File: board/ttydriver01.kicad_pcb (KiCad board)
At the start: 2 copper layers, 119.4 x 74.9 mm, 61 parts, among them J1 PRINTER JACK, J2 KEYBOARD JACK, J3 MOTOR CTL RELAY JACK, P1 CONN_01X02, SW1 Switch_SPDT, SW2 Button_SPDT, T1 Coilcraft-FA2469-AL, U1 NE555, U2 AP2553W6, U3 CP2102-breakout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

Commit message: First try at 2.1 autorouting
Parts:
- removed D12: 4.7V Zener, Diodes_SMD:SOD-123
- removed REF1, REF2, REF3, REF4: MountingHole_2.7mm_M2.5, Mounting_Holes:MountingHole_2.7mm_M2.5
- removed REF5: Fiducial_classic_Small_SilkscreenTop_Type1, Fiducials:Fiducial_classic_Small_SilkscreenTop_Type1
- added R17: 510, Resistors_SMD:R_1206, F.Cu at (145.5, 114.6)
- added R18: 2.2K, Resistors_SMD:R_1206, F.Cu at (159.8, 95.5)
- added W5: TEST_1P, Pin_Headers:Pin_Header_Straight_1x01_Pitch2.54mm, F.Cu at (127.3, 143.8)
- C2: footprint Capacitors_SMD:C_0805 -> Capacitors_ThroughHole:C_Disc_D6.0mm_W4.4mm_P5.00mm
- C8: value 880pf -> 910pf
- R6: value 720 -> 715
- R7: value 7.2K -> 7.15K
- W1, W2, W3, W4: footprint Connect:PINTST -> Pin_Headers:Pin_Header_Straight_1x01_Pitch2.54mm
- moved R16 50.0 mm to (148.3, 95.8), turned to 270 degrees
- moved T1 3.59 mm to (130.0, 123.4)
- moved U9 3.06 mm to (129.3, 136.7)
- moved C4 2.29 mm to (127.5, 131.8)
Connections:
- C1 pad 1: VCC -> Net-(C1-Pad1)
- C9 pad 1: VCC -> Net-(C1-Pad1)
- D13 pad 5: Net-(D12-Pad2) -> GND
- L3 pad 1: VCC -> Net-(C1-Pad1)
- R10 pad 2: Net-(D12-Pad1) -> /TxD
- R12 pad 2: VCC -> Net-(C1-Pad1)
- R5 pad 2: Net-(D12-Pad2) -> Net-(R5-Pad2)
- R6 pad 2: VCC -> Net-(C1-Pad1)
- U1 pad 4: VCC -> Net-(C1-Pad1)
- U1 pad 8: VCC -> Net-(C1-Pad1)
- U2 pad 6: VCC -> Net-(C1-Pad1)
- U3 pad 2-4: VCC -> Net-(C1-Pad1)
- U5 pad 2: VCC -> Net-(C1-Pad1)
- U6 pad 4: /RxD -> Net-(C1-Pad1)
- U6 pad 5: VCC -> /RxD
- U6 pad 6: /RxD -> Net-(C1-Pad1)
- U7 pad 1: Net-(U3-Pad3-5) -> Net-(R17-Pad2)
- U7 pad 2: GND -> Net-(U3-Pad3-5)
- U7 pad 4: VCC -> Net-(C1-Pad1)
- U7 pad 6: VCC -> Net-(C1-Pad1)
- U8 pad 2: VCC -> Net-(C1-Pad1)
- U8 pad 4: Net-(D12-Pad1) -> Net-(R5-Pad2)
- W1 pad 1: VCC -> Net-(C1-Pad1)
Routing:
- net GND: track 333.8 -> 0.00 mm, vias 1 -> 0
- net VCC: track 234.2 -> 0.00 mm, vias 3 -> 0
- net /HVNEG: track 180.0 -> 0.00 mm
- net Net-(J3-PadT): track 115.6 -> 0.00 mm
- net /ENABLE: track 106.9 -> 0.00 mm
- net Net-(J2-PadS): track 92.2 -> 0.00 mm, vias 1 -> 0
- net Net-(C3-Pad1): track 90.9 -> 0.00 mm, vias 2 -> 0
- net Net-(SW1-Pad2): track 72.2 -> 0.00 mm
- net Net-(R18-Pad1): track 70.1 -> 0.00 mm
- net Net-(R16-Pad1): track 62.5 -> 0.00 mm, vias 2 -> 0
- net Net-(D12-Pad2): track 58.3 -> 0.00 mm, vias 1 -> 0
- net /RxD: track 55.7 -> 0.00 mm
- net Net-(R13-Pad2): track 52.3 -> 0.00 mm, vias 2 -> 0
- net Net-(D12-Pad1): track 52.2 -> 0.00 mm, vias 1 -> 0
- net /TxD: track 51.6 -> 0.00 mm, vias 1 -> 0
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
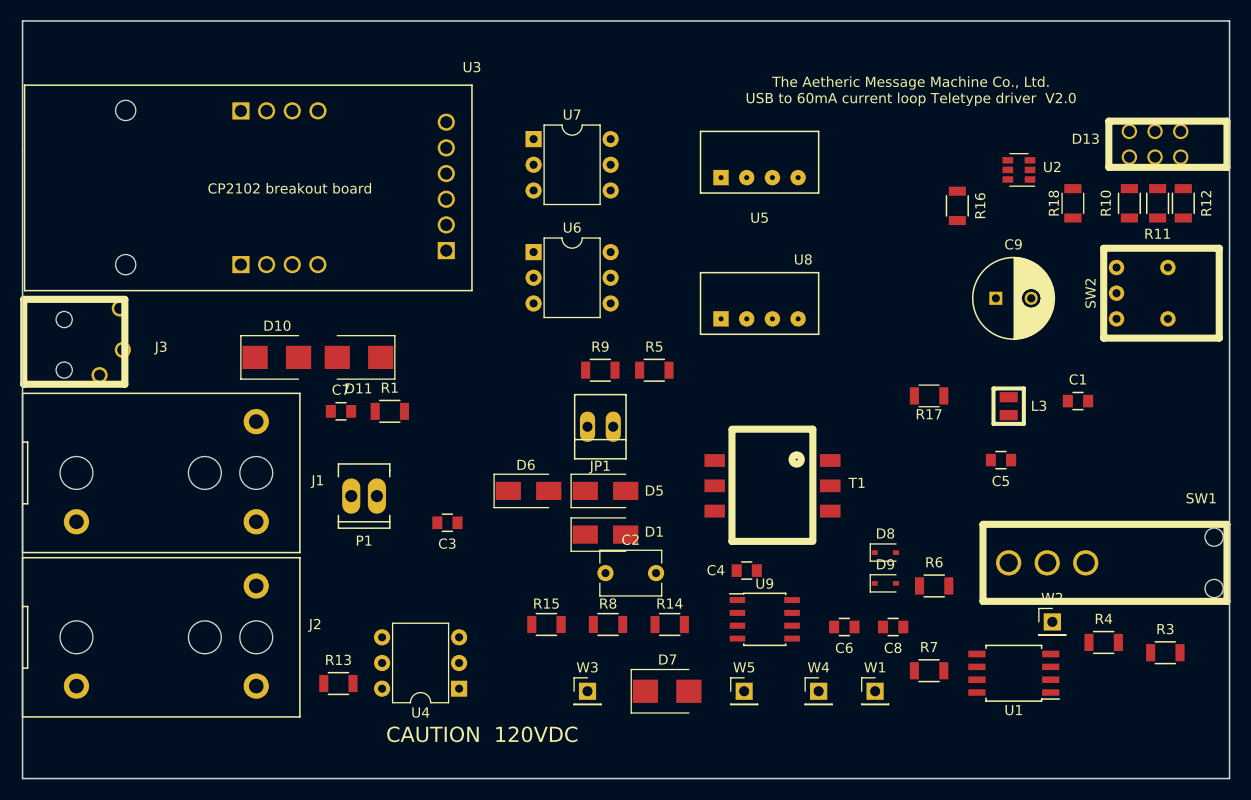
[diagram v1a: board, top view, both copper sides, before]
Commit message: Successful autoroute. Board lacks mounting holes
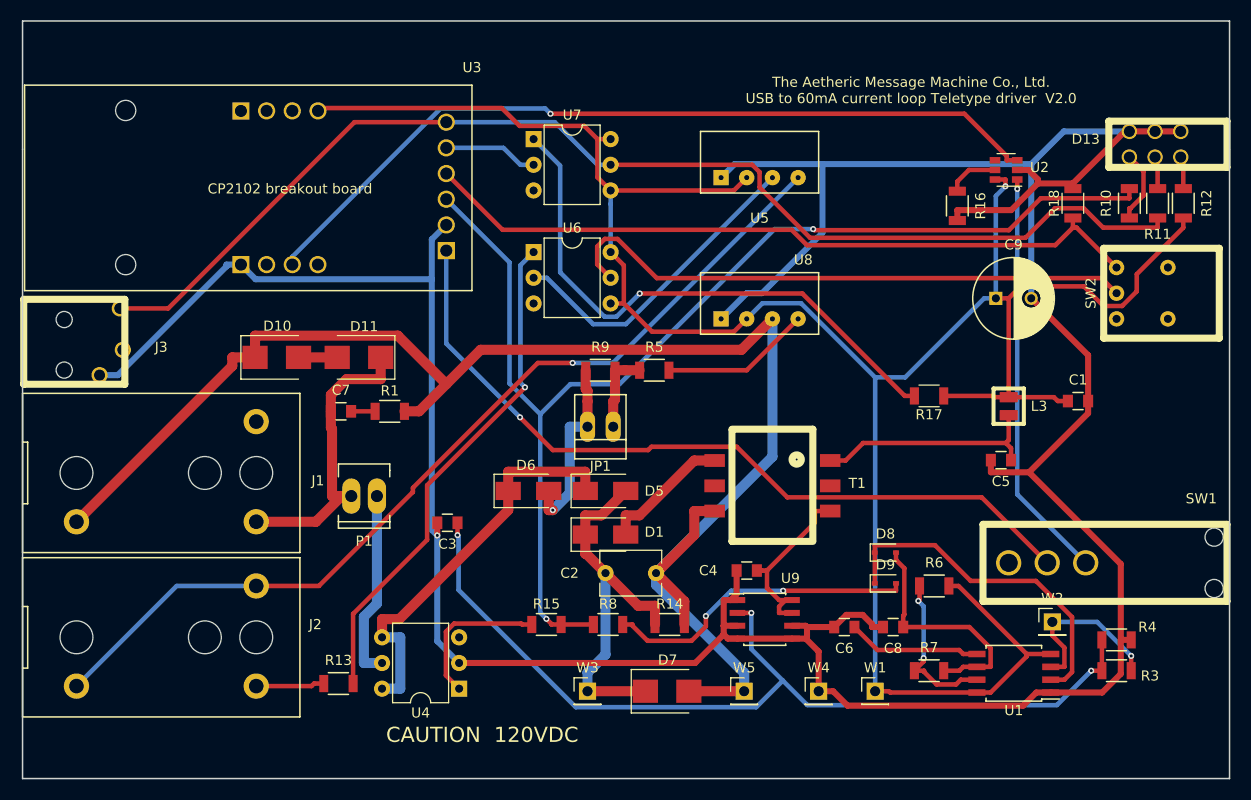
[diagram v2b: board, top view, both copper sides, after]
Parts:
- moved R3 5.14 mm to (164.1, 141.7)
- moved R4 1.30 mm to (164.1, 138.7)
- moved U2 1.27 mm to (153.2, 92.2)
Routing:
- net GND: track 0.00 -> 335.5 mm, vias 0 -> 1
- net Net-(C1-Pad1): track 0.00 -> 229.5 mm, vias 0 -> 1
- net /HVNEG: track 0.00 -> 154.8 mm
- net Net-(J3-PadT): track 0.00 -> 118.8 mm
- net /TxD: track 0.00 -> 118.7 mm, vias 0 -> 2
- net Net-(J2-PadS): track 0.00 -> 92.4 mm, vias 0 -> 1
- net Net-(C3-Pad1): track 0.00 -> 91.0 mm, vias 0 -> 3
- net /ENABLE: track 0.00 -> 80.9 mm, vias 0 -> 1
- net Net-(SW1-Pad2): track 0.00 -> 77.9 mm, vias 0 -> 1
- net Net-(R18-Pad1): track 0.00 -> 72.5 mm
- net /RxD: track 0.00 -> 57.5 mm
- net Net-(R17-Pad2): track 0.00 -> 56.3 mm, vias 0 -> 1
- net Net-(R13-Pad2): track 0.00 -> 50.4 mm, vias 0 -> 1
- net Net-(D5-Pad1): track 0.00 -> 40.7 mm
- net Net-(SW1-Pad1): track 0.00 -> 40.7 mm, vias 0 -> 1
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
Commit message: Successful autoroute. Mounting holes added.  Check further before fab.
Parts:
- added H1: MountingHole_2.5mm, Mounting_Holes:MountingHole_2.5mm, F.Cu at (61.0, 81.0)
- added H2: MountingHole_2.5mm, Mounting_Holes:MountingHole_2.5mm, F.Cu at (61.0, 148.6)
- added H3: MountingHole_2.5mm, Mounting_Holes:MountingHole_2.5mm, F.Cu at (170.2, 148.6)
- added H4: MountingHole_2.5mm, Mounting_Holes:MountingHole_2.5mm, F.Cu at (170.2, 81.0)
- moved R12 0.25 mm to (170.9, 95.5)
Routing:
- net /TxD: track 118.7 -> 135.2 mm, vias 2 -> 1
- net Net-(D9-Pad2): track 31.2 -> 44.3 mm, vias 2 -> 0
- net GND: track 335.5 -> 325.5 mm, vias 1 -> 2
- net Net-(C3-Pad1): track 91.0 -> 99.0 mm
- net Net-(R6-Pad1): track 16.0 -> 23.1 mm, vias 2 -> 0
- net Net-(D8-Pad1): track 34.1 -> 27.9 mm
- net /RxD: track 57.5 -> 52.3 mm, vias 0 -> 1
- net Net-(D6-Pad2): track 18.7 -> 14.6 mm, vias 1 -> 0
- net /OSC: track 16.9 -> 13.6 mm, vias 1 -> 0
- net Net-(SW1-Pad2): track 77.9 -> 74.6 mm
- net Net-(D5-Pad1): track 40.7 -> 37.7 mm
- net Net-(C1-Pad1): track 229.5 -> 227.1 mm, vias 1 -> 2
- net Net-(R17-Pad2): track 56.3 -> 58.5 mm
- net Net-(J3-PadT): track 118.8 -> 117.3 mm
- net Net-(SW1-Pad1): track 40.7 -> 42.2 mm
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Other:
- board text added: "The Aetheric Message Machine Co., Ltd. USB to 60mA current loop Teletype driver V2.1"
- board text removed: "The Aetheric Message Machine Co., Ltd. USB to 60mA current loop Teletype driver V2.0"

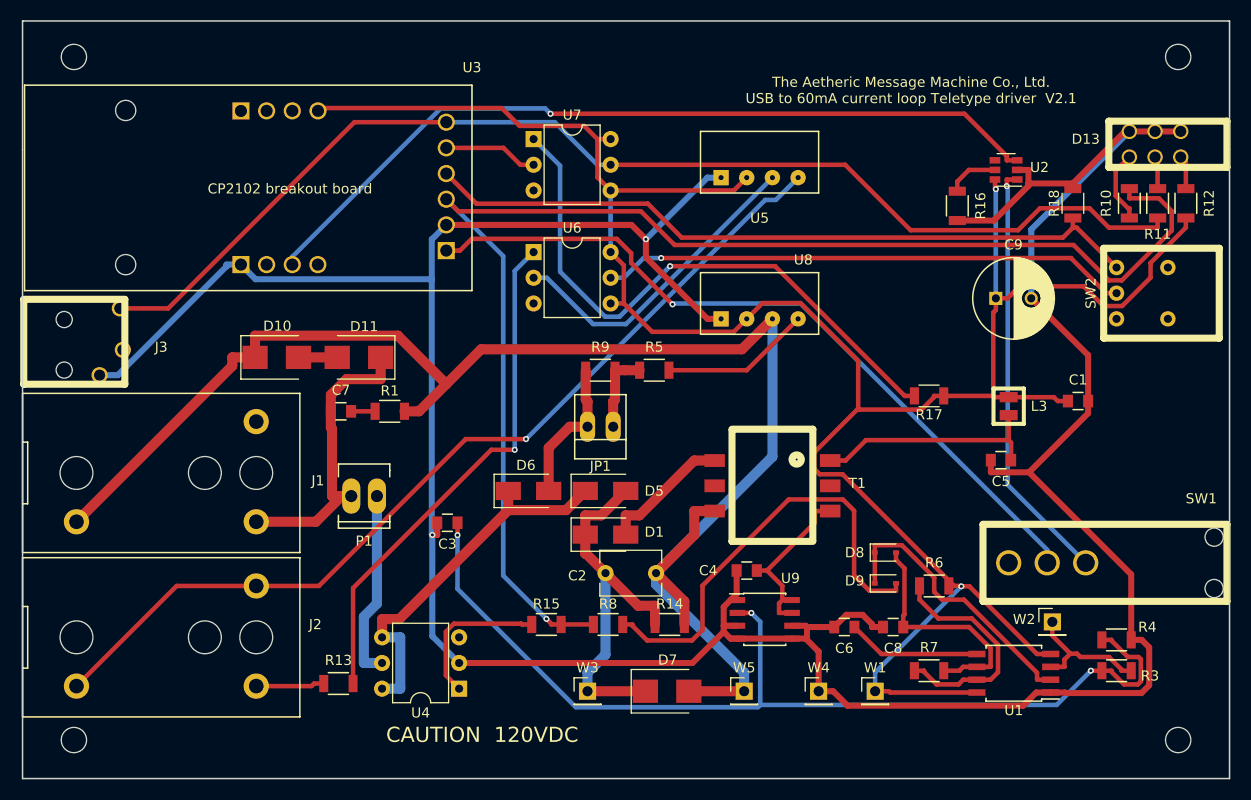
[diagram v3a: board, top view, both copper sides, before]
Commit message: BOM data updated. Next, final check before fab
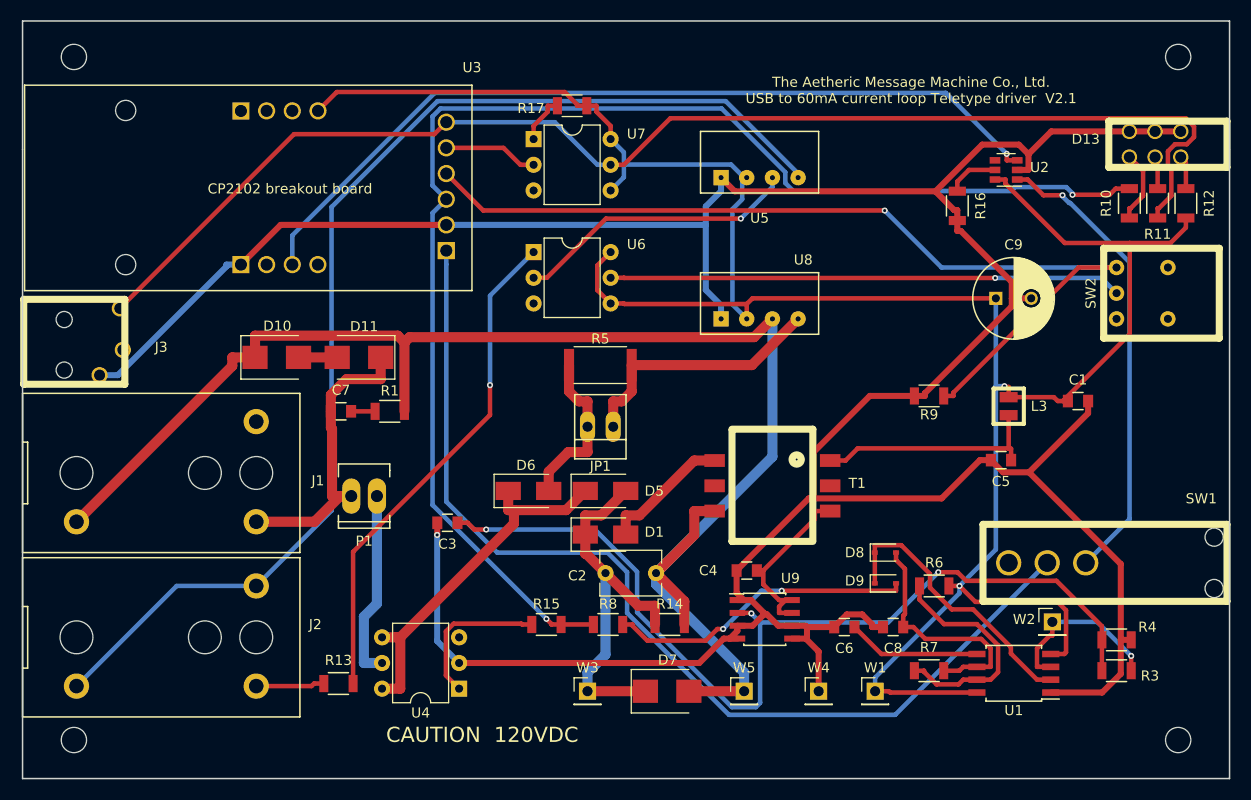
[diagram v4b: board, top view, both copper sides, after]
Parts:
- removed R18: 2.2K, Resistors_SMD:R_1206
- removed the R9 at (113.0, 112.0)
- added R17: 510, Resistors_SMD:R_1206, F.Cu at (110.2, 85.9)
- R15: value 680 -> 560
- R5: value 27 -> 150; footprint Resistors_SMD:R_1206 -> Resistors_SMD:R_2512
- R9: renamed from R17; value 510 -> 2.2K
- moved R5 5.36 mm to (113.0, 111.5)
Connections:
- R5 pad 1: Net-(JP1-Pad1) -> Net-(D6-Pad2)
- R5 pad 2: Net-(R5-Pad2) -> Net-(JP1-Pad1)
- R9 pad 1: Net-(C1-Pad1) -> Net-(R9-Pad1)
- R9 pad 2: Net-(R17-Pad2) -> GND
- SW2 pad 3: Net-(R18-Pad1) -> Net-(R9-Pad1)
- U3 pad 3-4: Net-(R18-Pad1) -> Net-(R9-Pad1)
- U8 pad 4: Net-(R5-Pad2) -> Net-(JP1-Pad1)
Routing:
- net Net-(R9-Pad1): track 0.00 -> 92.7 mm, vias 0 -> 1
- net Net-(R18-Pad1): track 71.9 -> 0.00 mm
- net Net-(R17-Pad2): track 58.5 -> 4.84 mm, vias 1 -> 0
- net Net-(SW1-Pad2): track 74.6 -> 101.6 mm, vias 1 -> 0
- net Net-(J2-PadS): track 92.2 -> 116.3 mm, vias 1 -> 0
- net Net-(JP1-Pad1): track 8.10 -> 25.7 mm
- net Net-(R5-Pad2): track 14.9 -> 0.00 mm
- net Net-(D9-Pad2): track 44.3 -> 30.5 mm, vias 0 -> 2
- net Net-(J3-PadT): track 117.3 -> 129.4 mm
- net Net-(C1-Pad1): track 227.1 -> 235.0 mm
- net GND: track 325.5 -> 332.6 mm, vias 2 -> 1
- net Net-(C3-Pad1): track 99.0 -> 93.1 mm
- net Net-(SW1-Pad1): track 42.2 -> 46.1 mm
- net /OSC: track 13.6 -> 17.2 mm, vias 0 -> 1
- net Net-(U5-Pad3): track 31.5 -> 28.3 mm, vias 0 -> 1
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
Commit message: Generated fab files with bigger via rings to pass DRC
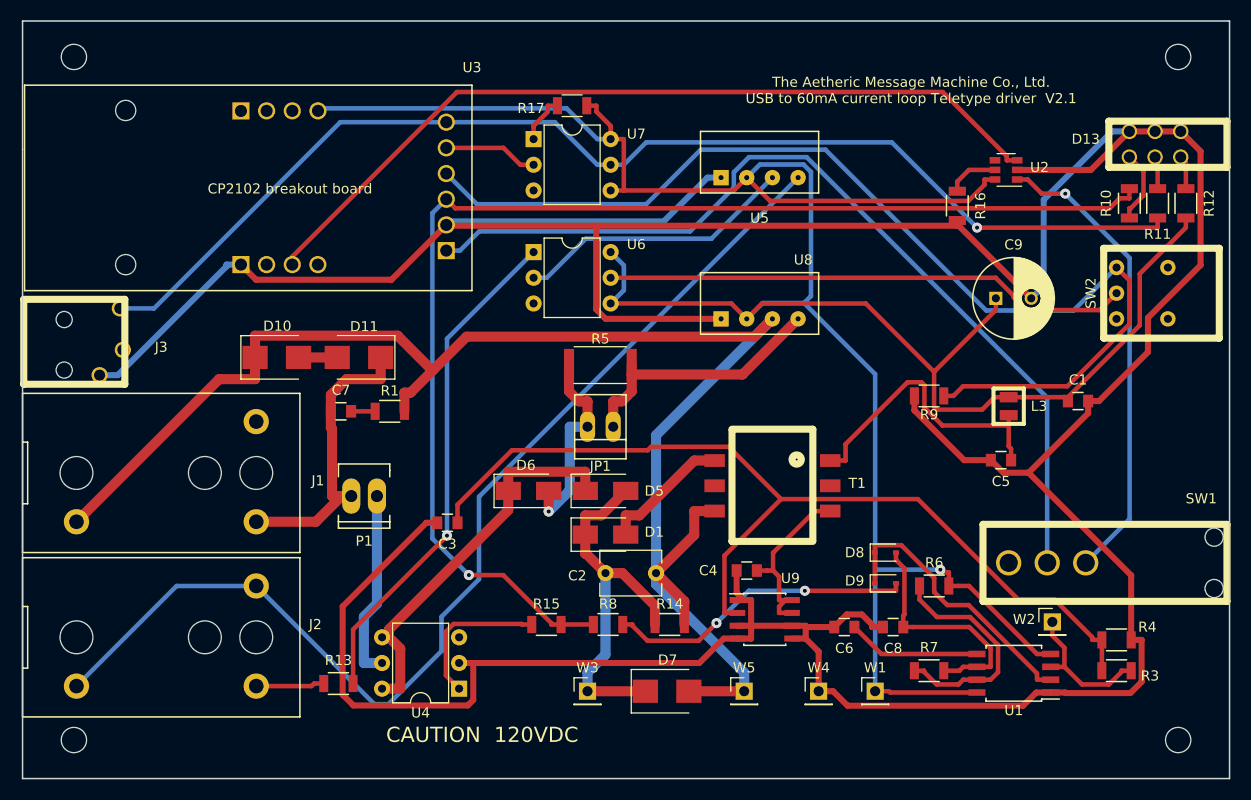
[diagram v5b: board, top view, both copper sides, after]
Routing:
- net GND: track 332.6 -> 410.5 mm, vias 1 -> 0
- net Net-(C1-Pad1): track 235.0 -> 274.3 mm, vias 2 -> 1
- net Net-(R9-Pad1): track 92.7 -> 105.6 mm, vias 1 -> 0
- net Net-(J3-PadT): track 129.4 -> 117.4 mm, vias 0 -> 1
- net /TxD: track 134.5 -> 122.9 mm, vias 2 -> 1
- net Net-(SW1-Pad2): track 101.6 -> 90.3 mm
- net Net-(J2-PadS): track 116.3 -> 108.7 mm
- net Net-(C5-Pad1): track 22.8 -> 29.4 mm
- net Net-(D6-Pad2): track 16.4 -> 20.4 mm, vias 0 -> 1
- net /OSC: track 17.2 -> 14.3 mm, vias 1 -> 0
- net Net-(D5-Pad1): track 36.2 -> 38.8 mm
- net /HVNEG: track 152.9 -> 154.7 mm
- net /RxD: track 50.7 -> 52.1 mm, vias 1 -> 0
- net /ENABLE: track 83.6 -> 82.3 mm, vias 1 -> 0
- net Net-(C3-Pad1): track 93.1 -> 93.9 mm, vias 3 -> 0
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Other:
- net class Default: via_dia 0.6 -> 1
- net class HV: via_dia 0.6 -> 1
- net class PWR: via_dia 0.6 -> 1
- rule via_min_size: 0.4 -> 0.5

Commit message: V2.2 board fixes on PCB
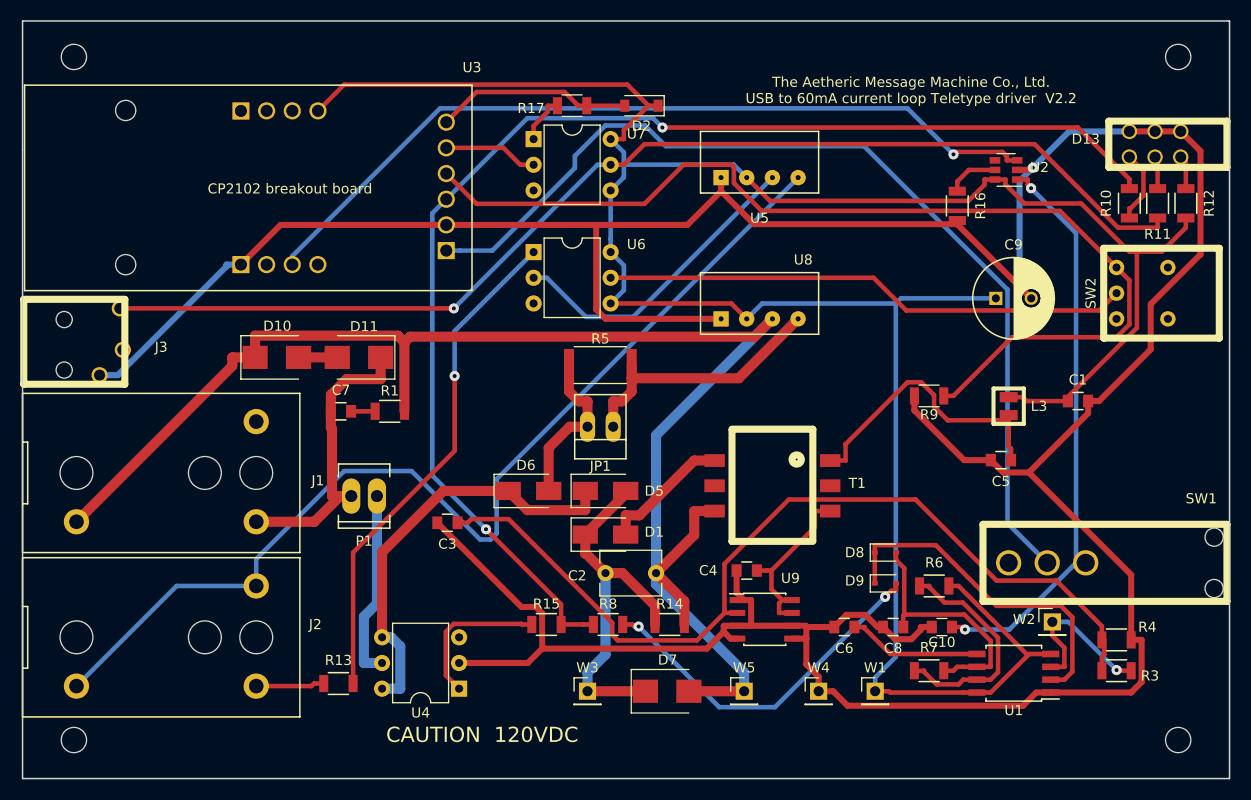
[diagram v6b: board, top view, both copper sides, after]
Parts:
- added C10: 0.1uF, Capacitors_SMD:C_0805, F.Cu at (146.8, 137.4)
- added D2: 1.8V, Diodes_SMD:D_SOD-123, F.Cu at (117.1, 85.9)
- D10, D11, D7: value D_Zener -> 120V
- R9: value 2.2K -> 1K
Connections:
- R17 pad 1: Net-(C1-Pad1) -> Net-(D2-Pad2)
- U3 pad 3-6: Net-(J3-PadT) -> Net-(D2-Pad2)
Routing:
- net GND: track 410.5 -> 361.1 mm, vias 0 -> 1
- net Net-(D2-Pad2): track 0.00 -> 19.5 mm
- net Net-(C1-Pad1): track 274.3 -> 255.3 mm, vias 1 -> 0
- net Net-(C10-Pad1): track 46.3 -> 57.0 mm, vias 1 -> 2
- net Net-(SW1-Pad2): track 90.3 -> 96.7 mm
- net Net-(D8-Pad1): track 27.9 -> 34.1 mm
- net Net-(J2-PadS): track 108.7 -> 102.5 mm
- net Net-(D9-Pad2): track 30.5 -> 35.9 mm
- net Net-(C3-Pad1): track 93.9 -> 89.4 mm
- net Net-(D6-Pad2): track 20.4 -> 16.3 mm, vias 1 -> 0
- net Net-(R9-Pad1): track 105.6 -> 101.7 mm
- net Net-(J3-PadT): track 117.4 -> 113.8 mm
- net Net-(U5-Pad3): track 27.7 -> 30.9 mm
- net Net-(D5-Pad1): track 38.8 -> 41.9 mm
- net /TxD: track 122.9 -> 125.4 mm, vias 1 -> 2
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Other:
- board text added: "The Aetheric Message Machine Co., Ltd. USB to 60mA current loop Teletype driver V2.2"
- board text removed: "The Aetheric Message Machine Co., Ltd. USB to 60mA current loop Teletype driver V2.1"

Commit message: Reeady to go to fab
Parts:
- moved W2 14.0 mm to (145.5, 143.8)
- moved R7 6.51 mm to (151.6, 144.0), turned to 180 degrees
- moved U1 2.96 mm to (155.4, 139.4)
- moved W4 1.27 mm to (133.3, 143.8)
- moved W1 0.76 mm to (139.4, 143.8)
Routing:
- net /TxD: track 125.4 -> 160.7 mm, vias 2 -> 1
- net GND: track 361.1 -> 395.1 mm
- net Net-(J3-PadT): track 113.8 -> 130.5 mm, vias 1 -> 0
- net /OSC: track 16.1 -> 27.7 mm, vias 1 -> 0
- net Net-(D9-Pad2): track 35.9 -> 44.3 mm, vias 2 -> 0
- net /RxD: track 52.1 -> 59.8 mm
- net Net-(C5-Pad1): track 28.6 -> 22.9 mm
- net Net-(R15-Pad1): track 15.0 -> 10.7 mm
- net Net-(C3-Pad1): track 89.4 -> 93.4 mm
- net Net-(C8-Pad1): track 24.7 -> 28.4 mm
- net Net-(U5-Pad3): track 30.9 -> 27.7 mm
- net /ENABLE: track 81.2 -> 78.0 mm, vias 1 -> 0
- net Net-(R9-Pad1): track 101.7 -> 99.3 mm, vias 0 -> 1
- net Net-(D8-Pad1): track 34.1 -> 31.7 mm
- net Net-(SW1-Pad2): track 96.7 -> 94.4 mm
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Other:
- board text added: "Jumper IN for 55 ohm selector"
- board text added: "Loop current meter or jumper"
